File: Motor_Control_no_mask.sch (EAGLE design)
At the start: 33 parts

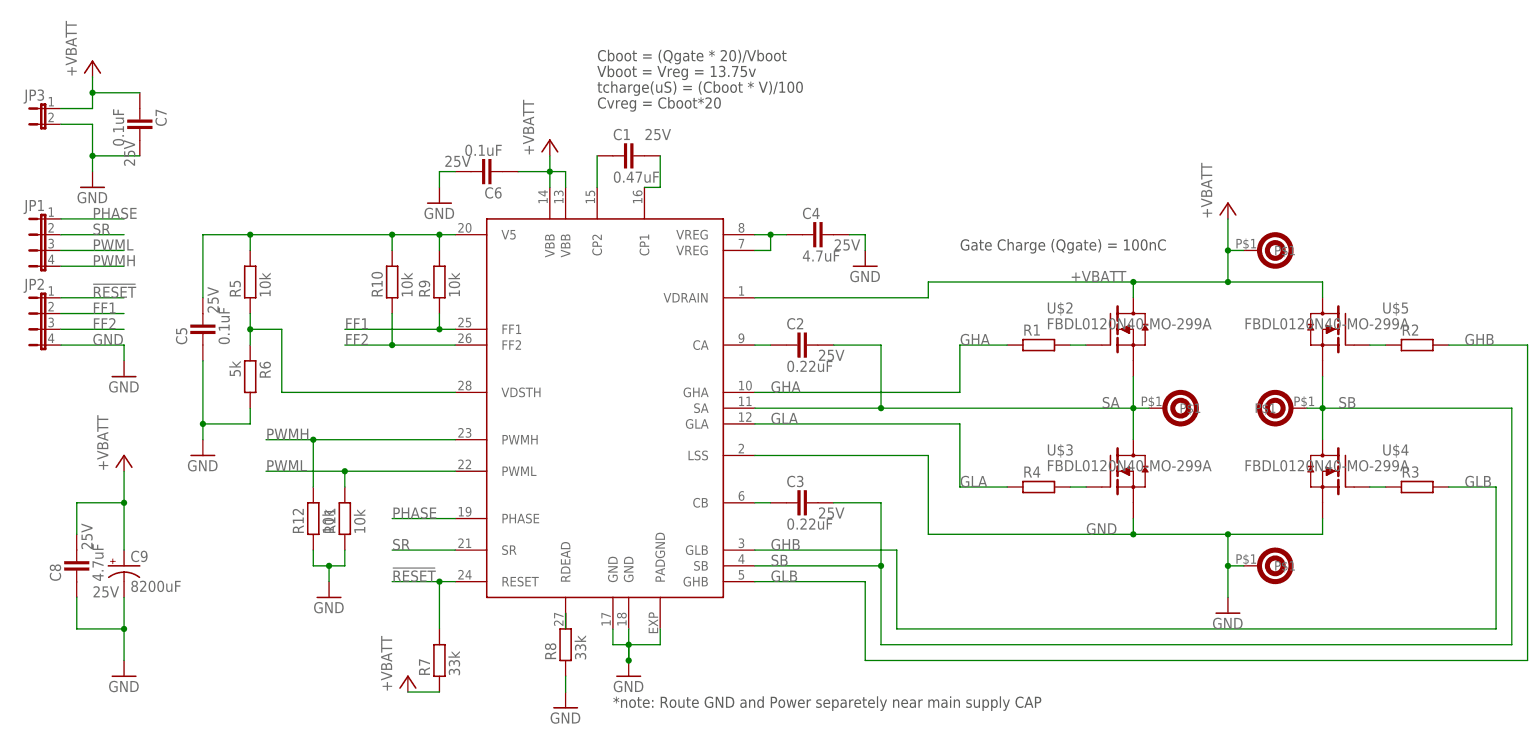
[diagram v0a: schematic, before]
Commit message: Fixed the solder mask and Gate resistors
The soldermask on the bottom side has been changed so there is at least
20 mils covering the traces. this should prevent shorts.
The gate resistors are now 4.7 Ohm. I'm not 100% sure this is correct,
might change to 10 Ohm if I see issues.
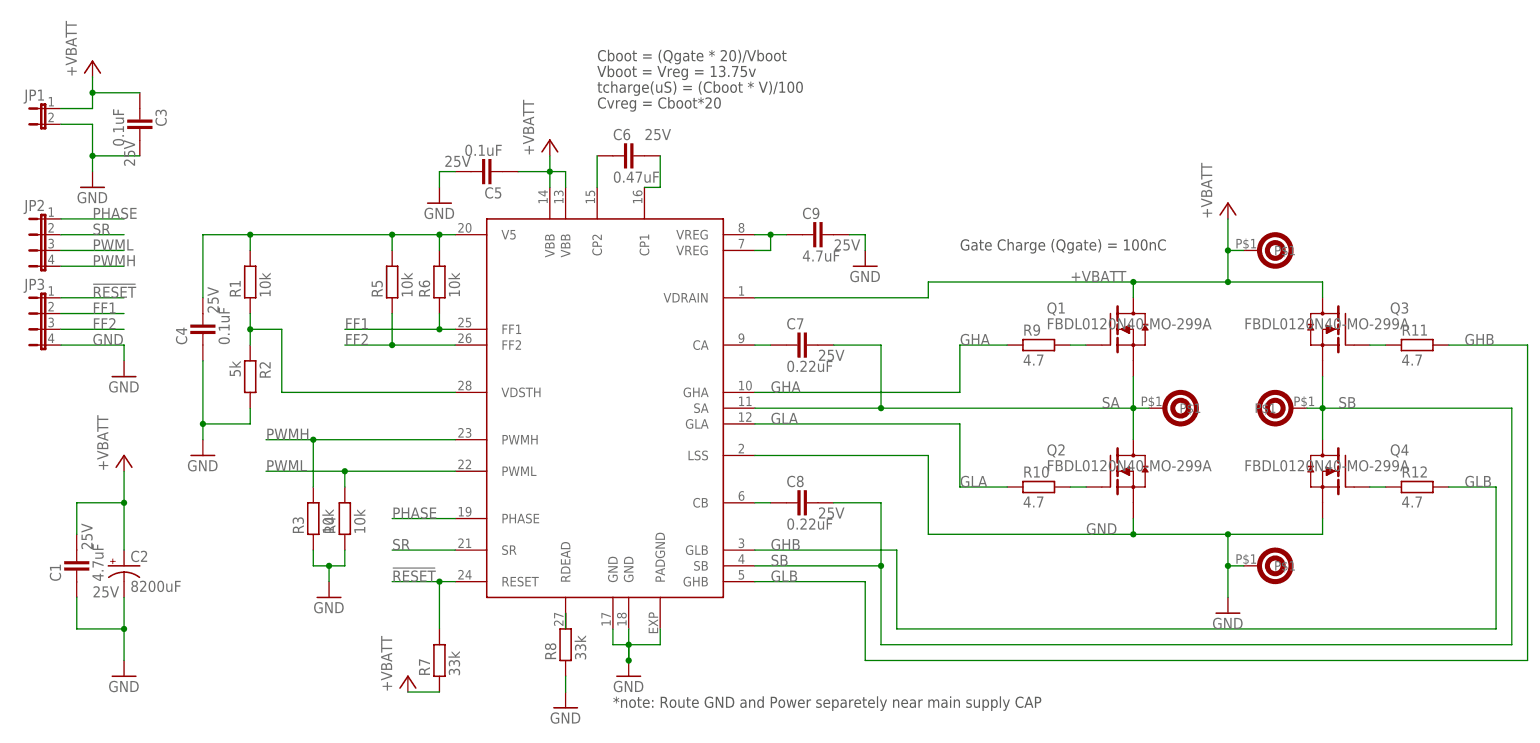
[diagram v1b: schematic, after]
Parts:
- C1: value 0.47uF -> 4.7uF
- C2: value 0.22uF -> 8200uF; device Motor_Control:CAPACITOR_0603L -> Motor_Control:CPOL-US-PTH-10-22
- C3: value 0.22uF -> 0.1uF; device Motor_Control:CAPACITOR_0603L -> Motor_Control:CAPACITOR_0603
- C4: value 4.7uF -> 0.1uF; device Motor_Control:CAPACITOR_0603 -> Motor_Control:CAPACITOR_0603L
- C5: device Motor_Control:CAPACITOR_0603L -> Motor_Control:CAPACITOR_0603
- C6: value 0.1uF -> 0.47uF
- C7: value 0.1uF -> 0.22uF; device Motor_Control:CAPACITOR_0603 -> Motor_Control:CAPACITOR_0603L
- C8: value 4.7uF -> 0.22uF; device Motor_Control:CAPACITOR_0603 -> Motor_Control:CAPACITOR_0603L
- C9: value 8200uF -> 4.7uF; device Motor_Control:CPOL-US-PTH-10-22 -> Motor_Control:CAPACITOR_0603
- JP1: device Motor_Control:JP4E -> Motor_Control:JP1E
- JP3: device Motor_Control:JP1E -> Motor_Control:JP4E
- R1, R3, R4: value (none) -> 10k
- R10, R11, R12, R9: value 10k -> 4.7
- R2: value (none) -> 5k
- R6: value 5k -> 10k
- renumbered U$1 to U1, U$2 to Q1, U$3 to Q2, U$4 to Q4, U$5 to Q3, U$6 to J2, U$7 to J4, U$8 to J1, U$9 to J3
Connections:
- net !RESET: now also JP3.1; no longer JP2.1
- net +VBATT: now also C1.2, C2.+, C3.1, C5.1, JP1.1; no longer C6.1, C7.1, C8.2, C9.+, JP3.1
- net FF1: now also JP3.2, R6.1; no longer JP2.2, R9.1
- net FF2: now also JP3.3, R5.1; no longer JP2.3, R10.1
- net GHA: now also R9.1; no longer R1.1
- net GHB: now also R11.2; no longer R2.2
- net GLA: now also R10.1; no longer R4.1
- net GLB: now also R12.2; no longer R3.2
- net GND: now also C1.1, C2.-, C3.2, C4.1, C5.2, C9.2, JP1.2, JP3.4, R2.2, R3.1, R4.1; no longer C4.2, C5.1, C6.2, C7.2, C8.1, C9.-, JP2.4, JP3.2, R11.1, R12.1, R6.2
- net N$1: now also R9.2; no longer R1.2
- net N$13: now also R1.1, R2.1; no longer R5.1, R6.1
- net N$15: now also C8.1; no longer C3.1
- net N$19: now also C6.1; no longer C1.1
- net N$2: now also R10.2; no longer R4.2
- net N$20: now also C6.2; no longer C1.2
- net N$3: now also R12.1; no longer R3.1
- net N$4: now also R11.1; no longer R2.1
- net N$5: now also C9.1; no longer C4.1
- net N$6: now also C7.1; no longer C2.1
- net PHASE: now also JP2.1; no longer JP1.1
- net PWMH: now also JP2.4, R3.2; no longer JP1.4, R12.2
- net PWML: now also JP2.3, R4.2; no longer JP1.3, R11.2
- net SA: now also C7.2; no longer C2.2
- net SB: now also C8.2; no longer C3.2
- net SR: now also JP2.2; no longer JP1.2
- net V5: now also C4.2, R1.2, R6.2; no longer C5.2, R10.2, R9.2
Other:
- moved on the sheet: C1, C3, C4, C5, C6, C7, C8, JP2, R1, R10, R11, R12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
